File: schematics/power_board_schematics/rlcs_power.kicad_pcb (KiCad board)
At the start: 2 copper layers, 56.9 x 106.7 mm, 52 parts, among them J1 SD_Card, J10 Conn_14_to_21, J11 conn_power, J12 conn_A8_to_A15, J13 conn_A0_to_A7, J14 conn_22_to_53, J2 Conn_01x05_Male, J3 Conn_01x05_Male, J4 Battery Conn, J5 CONN_01X02, J6 CONN_01X02, J7 CONN_01X02, J8 Conn_0_to_7, J9 conn_8_to_13, Q1 Q_NPN_BEC, Q2 Q_NPN_BEC, T1 12 to 3v3, T2 12 to 5

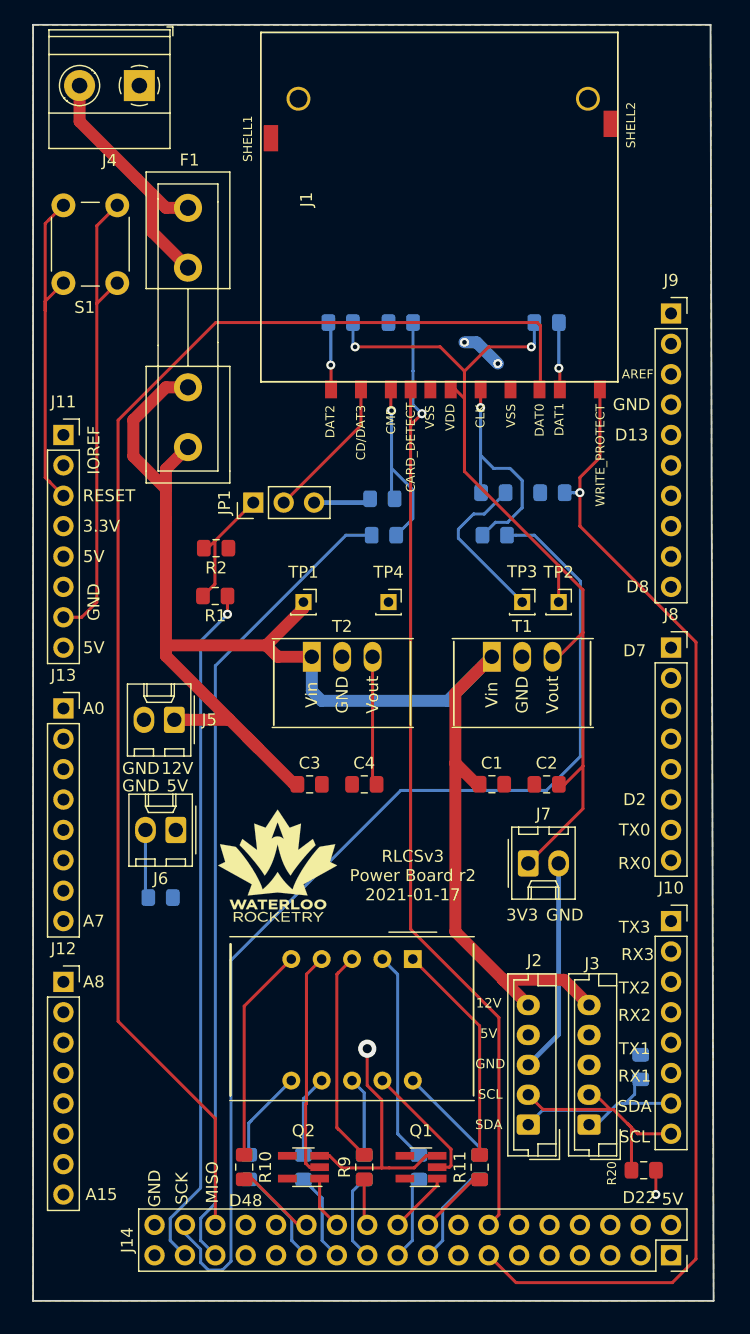
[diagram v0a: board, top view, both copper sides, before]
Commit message: Update footprint resistors
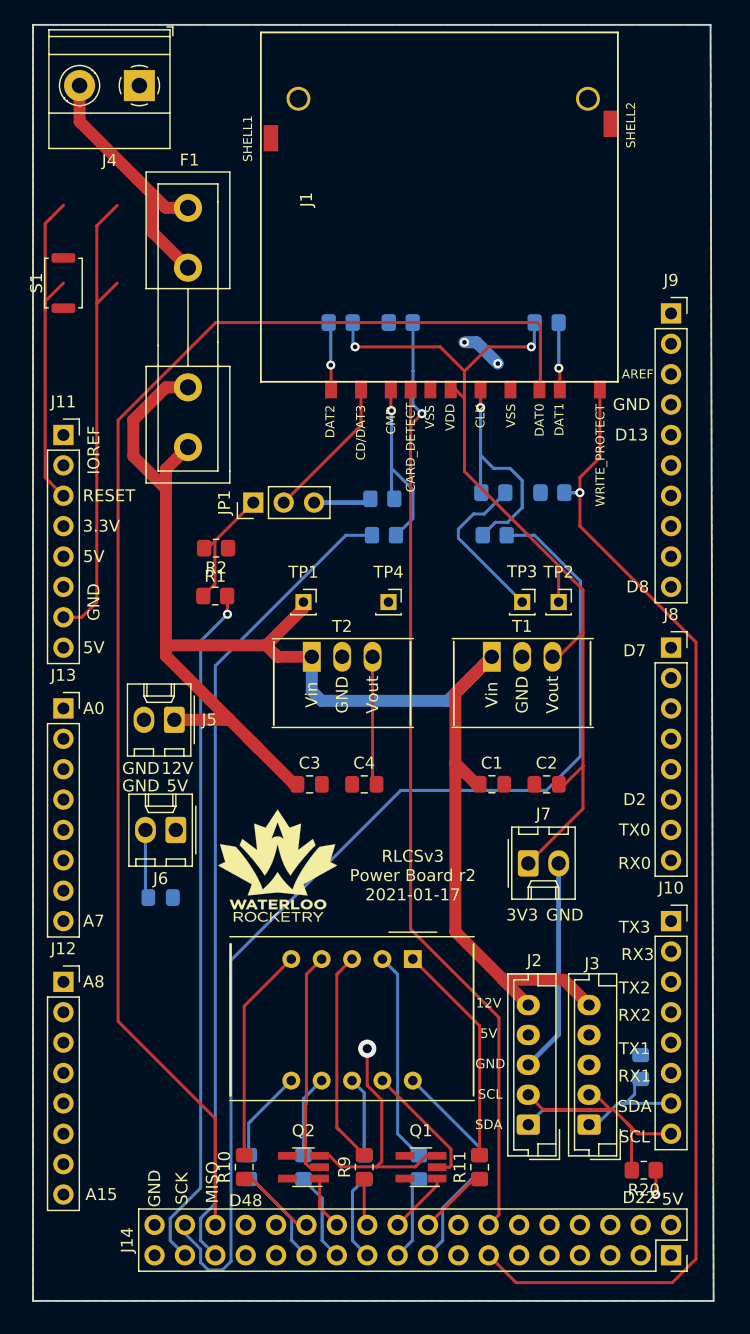
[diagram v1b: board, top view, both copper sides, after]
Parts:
- R1, R10, R11, R12, R13, R14, R15, R16, R17, R18, R19, R2, R20, R3, R4, R5, R6, R7, R8, R9: footprint Resistor_SMD:R_0805_2012Metric_Pad1.15x1.40mm_HandSolder -> Resistor_SMD:R_0805_2012Metric_Pad1.20x1.40mm_HandSolder
- S1: footprint Button_Switch_THT:SW_PUSH_6mm -> Button_Switch_SMD:SW_Push_SPST_NO_Alps_SKRK
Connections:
- net ARD_CON_SD_SCL renamed ARD_CON_SD_SCK

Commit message: fix silk screens that broke from chaning footprints
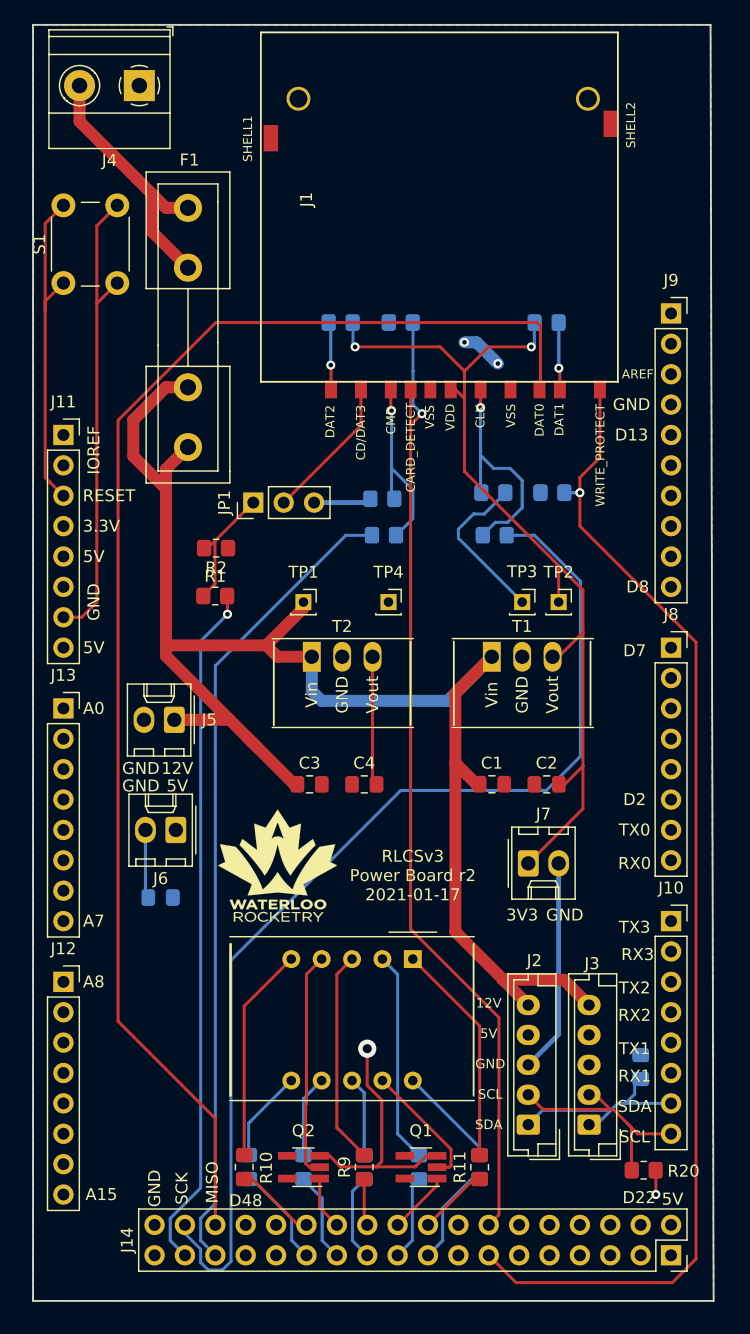
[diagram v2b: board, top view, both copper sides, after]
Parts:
- S1: footprint Button_Switch_SMD:SW_Push_SPST_NO_Alps_SKRK -> Button_Switch_THT:SW_PUSH_6mm

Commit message: fininish labelling connectors and export gerbers
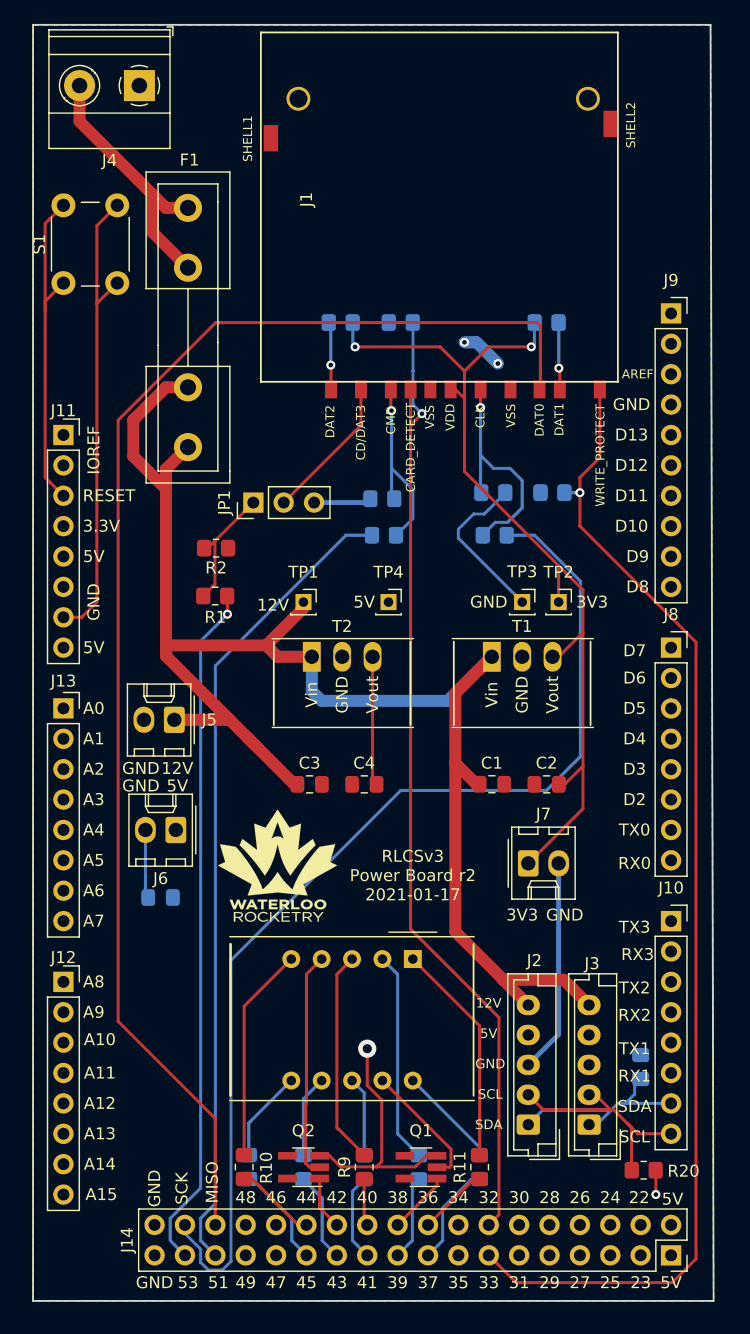
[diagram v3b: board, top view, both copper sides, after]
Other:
- board text added: "12V"
- board text added: "3V3"
- board text added: "5V"
- board text added: "GND"

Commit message: Add voltage sensing, fix transistor footprint and redo shield (#30)
* Add voltage sensing, fix transistor footprint and redo shield

* Added resistors to transistors, generate pdf and gerbers

* Review fixes

* Make 12V traces support higher current, review fixes
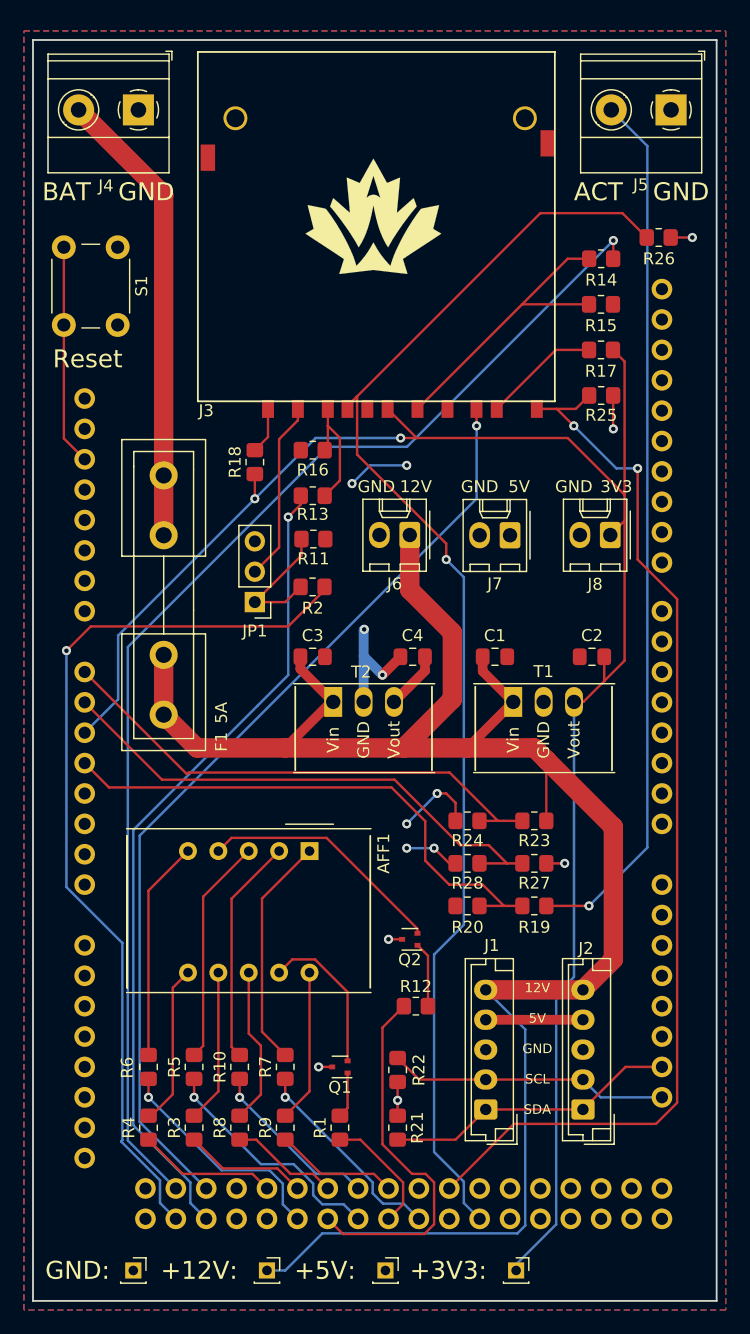
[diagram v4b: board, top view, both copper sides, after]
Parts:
- removed the C4 at (103.4, 133.9)
- removed the G*** at (113.2, 131.3)
- removed J10: Conn_14_to_21, Connector_PinSocket_2.54mm:PinSocket_1x08_P2.54mm_Vertical
- removed J11: conn_power, Connector_PinSocket_2.54mm:PinSocket_1x08_P2.54mm_Vertical
- removed J12: conn_A8_to_A15, Connector_PinSocket_2.54mm:PinSocket_1x08_P2.54mm_Vertical
- removed J13: conn_A0_to_A7, Connector_PinSocket_2.54mm:PinSocket_1x08_P2.54mm_Vertical
- removed J14: conn_22_to_53, Connector_PinSocket_2.54mm:PinSocket_2x18_P2.54mm_Vertical
- removed the J8 at (146.1, 113.0)
- removed J9: conn_8_to_13, Connector_PinSocket_2.54mm:PinSocket_1x10_P2.54mm_Vertical
- added G***: LOGO, rlcs_power_footprints:rocketry_logo_small_noletters, F.Cu at (121.2, 77.0)
- added G***: LOGO, rlcs_power_footprints:rocketry_logo_small_noletters, B.Cu at (131.6, 77.7)
- added J5: Battery Conn, TerminalBlock_Phoenix:TerminalBlock_Phoenix_MKDS-1,5-2_1x02_P5.00mm_Horizontal, F.Cu at (146.1, 68.1)
- added R1: 5k, Resistor_SMD:R_0805_2012Metric_Pad1.20x1.40mm_HandSolder, F.Cu at (118.4, 153.2)
- added R12: 5k, Resistor_SMD:R_0805_2012Metric_Pad1.20x1.40mm_HandSolder, F.Cu at (124.7, 143.0)
- added R19: 20k, Resistor_SMD:R_0805_2012Metric_Pad1.20x1.40mm_HandSolder, F.Cu at (134.6, 134.6)
- added R20: 10k, Resistor_SMD:R_0805_2012Metric_Pad1.20x1.40mm_HandSolder, F.Cu at (129.0, 134.6)
- added R23: 20k, Resistor_SMD:R_0805_2012Metric_Pad1.20x1.40mm_HandSolder, F.Cu at (134.6, 127.5)
- added R24: 10k, Resistor_SMD:R_0805_2012Metric_Pad1.20x1.40mm_HandSolder, F.Cu at (129.0, 127.5)
- added R27: 10k, Resistor_SMD:R_0805_2012Metric_Pad1.20x1.40mm_HandSolder, F.Cu at (134.6, 131.1)
- added R28: 10k, Resistor_SMD:R_0805_2012Metric_Pad1.20x1.40mm_HandSolder, F.Cu at (129.0, 131.1)
- added XA1: Arduino_Mega2560_Shield, rlcs_power_footprints:Arduino_Mega2560_Shield, F.Cu at (94.5, 64.3)
- Q1, Q2: footprint Package_TO_SOT_SMD:SOT-23-5_HandSoldering -> Package_TO_SOT_SMD:SOT-523
- R10: renamed from R14; moved to F.Cu
- R13: renamed from R3; moved to F.Cu
- R14: renamed from R4; moved to F.Cu
- R15: renamed from R5; moved to F.Cu
- R16: renamed from R6; moved to F.Cu
- R17: renamed from R15; moved to F.Cu
- R18: renamed from R16; moved to F.Cu
- R21: renamed from R19; moved to F.Cu
- R25: renamed from R17; moved to F.Cu
- R26: renamed from R18; moved to F.Cu
- R3: renamed from R7; moved to F.Cu
- R4: renamed from R8; moved to F.Cu
- R8: renamed from R12; moved to F.Cu
- R9: renamed from R13; moved to F.Cu
- moved TP3 64.6 mm to (101.1, 165.1)
- moved TP2 56.0 mm to (133.1, 165.1)
- moved TP1 56.0 mm to (112.3, 165.1)
- moved TP4 55.9 mm to (122.2, 165.1)
- moved J7 37.3 mm to (132.6, 103.6)
- moved J8 28.3 mm to (141.0, 103.6), turned to 180 degrees
- moved J6 25.0 mm to (124.2, 103.6)
- moved R14 24.8 mm to (140.2, 80.5)
- moved R26 22.7 mm to (145.0, 78.7), turned to 180 degrees
- moved F1 22.5 mm to (103.6, 98.6)
- moved R22 22.2 mm to (123.2, 148.3), turned to 90 degrees
- moved Q2 21.0 mm to (124.2, 137.4)
- moved R21 20.9 mm to (123.2, 153.2)
- moved R7 18.3 mm to (113.8, 148.1)
- moved R15 18.1 mm to (140.2, 84.3)
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- renumbered J2 to J1, J3 to J2, J1 to J3, J5 to J6, J6 to J7, J7 to J8, R2 to R11, R1 to R2, R20 to R22, R9 to R5, R10 to R6, R11 to R7
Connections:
- net +3V3 renamed SENSE_3V
- Q1 pad 1: Sevenseg_D2 -> Net-(Q1-Pad1)
- Q2 pad 1: Sevenseg_D1 -> Net-(Q2-Pad1)
- S1 pad 1: Net-(J11-Pad2) -> GND
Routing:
- net /ACTUATOR_BAT: track 0.00 -> 73.4 mm, vias 0 -> 1
- net SENSE_3V: track 79.8 -> 151.2 mm
- net SENSE_ACTUATOR: track 0.00 -> 45.5 mm
- net SENSE_5V: track 0.00 -> 44.5 mm
- net SENSE_12V: track 0.00 -> 43.4 mm
- net ARD_CON_SD_MISO: track 114.8 -> 79.1 mm, vias 0 -> 1
- net Net-(J11-Pad2): track 28.8 -> 0.00 mm
- net Sevenseg_D1: track 4.47 -> 31.2 mm
- net +12V: track 134.3 -> 160.3 mm
- net ARD_CON_SD_CD: track 82.7 -> 107.8 mm
- net Net-(S1-Pad2): track 39.6 -> 18.4 mm
- net GND: track 46.0 -> 27.2 mm, vias 2 -> 8
- net ARD_CON_SD_SS: track 57.6 -> 75.3 mm
- net Sevenseg_E: track 3.92 -> 20.0 mm, vias 0 -> 1
- net Net-(F1-Pad1): track 22.4 -> 38.5 mm
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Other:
- board size 56.9 x 106.7 mm -> 57.2 x 105.4 mm
- net class 15volt removed
- net class Default removed
- net class battery removed
- board text added: "+12V:"
- board text added: "+3V3:"
- board text added: "+5V:"
- board text added: "5A"
- board text added: "ACT"
- board text added: "BAT"
- board text added: "GND:"
- board text added: "RLCSv3 Power Board {dblquote}The Juice{dblquote} R3 2022-01-27 Jack Christensen"
- board text added: "Reset"
- board text removed: "12V"
- board text removed: "3V3"
- board text removed: "5V"
- board text removed: "RLCSv3 Power Board r2 2021-01-17"
